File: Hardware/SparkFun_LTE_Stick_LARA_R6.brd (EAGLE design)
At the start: 25.4 x 82.5 mm, 133 parts, among them IC1 SN74AVC4T774PW, IC3 SN74AVC4T774PW, J1 NANO_SIM, U1 LARA-R6401, U2 AP7361C-33

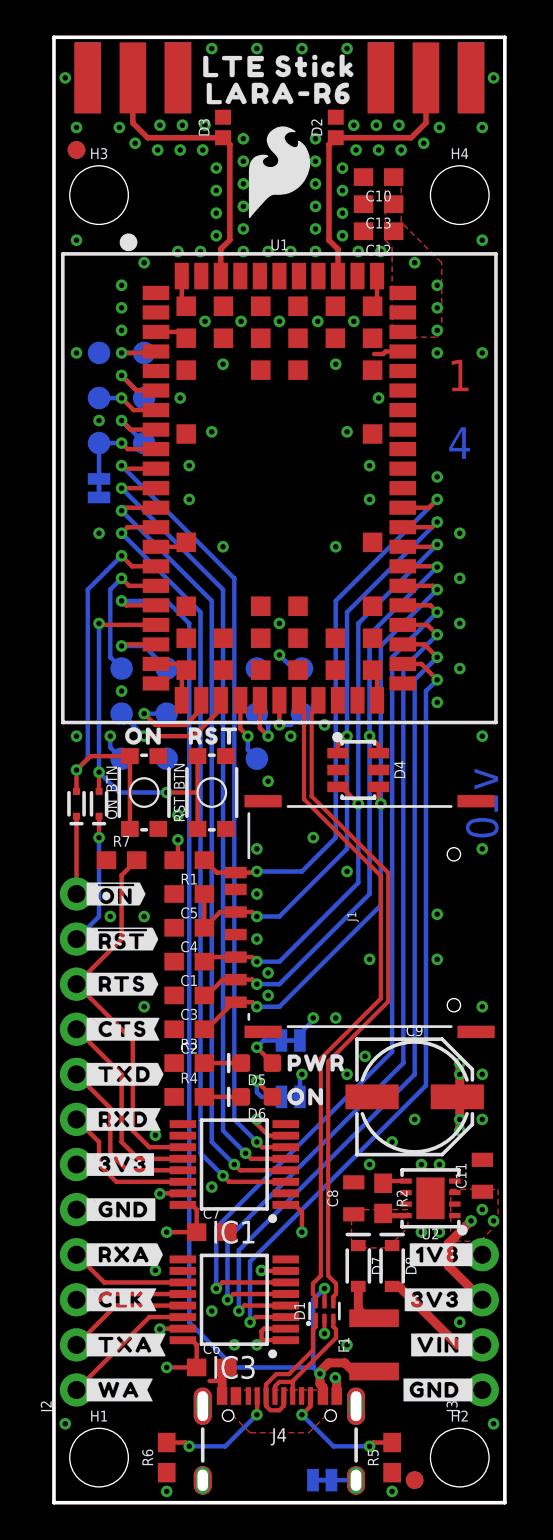
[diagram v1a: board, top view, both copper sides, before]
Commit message: v11 - Label SMA connectors in silkscreen
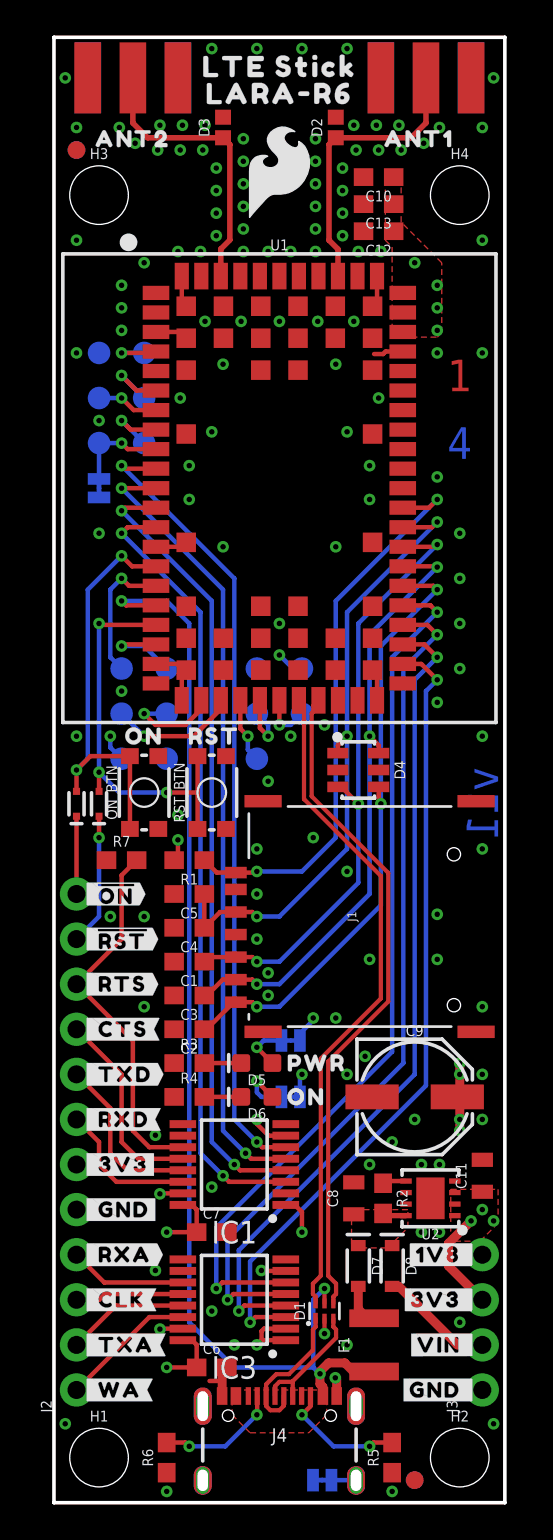
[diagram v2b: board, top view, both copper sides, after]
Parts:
- added U$29, U$36: (no value), output:ANT10
- added U$61, U$62: (no value), output:ANT20
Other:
- board text added: "v11"
- board text removed: "v10"
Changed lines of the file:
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@@
 <dimension x1="0" y1="0" x2="0" y2="73.66" x3="-8.89" y3="36.83" textsize="1.778" textratio="15" layer="47" unit="inch"/>
 <dimension x1="0" y1="0" x2="0" y2="82.55" x3="-12.7" y3="41.275" textsize="1.778" textratio="15" layer="47" unit="inch"/>
-<text x="24.13" y="39.37" size="1.778" layer="16" font="vector" ratio="15" rot="SMR270" align="center">v10</text>
+<text x="24.13" y="39.37" size="1.778" layer="16" font="vector" ratio="15" rot="SMR270" align="center">v11</text>
 <text x="22.86" y="63.5" size="1.778" layer="1" font="vector" ratio="15" rot="SR0" align="center">1</text>
 <text x="22.86" y="62.23" size="1.778" layer="2" font="vector" ratio="15" rot="SR0" align="center">2</text>
@@
 <element name="FRAME1" library="SparkFun-Aesthetics" package="CREATIVE_COMMONS" value="FRAME-LEDGER" x="-10.16" y="-25.4" smashed="yes">
 <attribute name="DESIGNER" value="Dryw Wade" x="-10.16" y="-25.4" size="1.778" layer="27" display="off"/>
-<attribute name="REV" value="v10" x="-10.16" y="-25.4" size="1.778" layer="27" display="off"/>
+<attribute name="REV" value="v11" x="-10.16" y="-25.4" size="1.778" layer="27" display="off"/>
 </element>
 <element name="U$56" library="output" package="UART20" value="" x="3.81" y="66.675" smashed="yes" rot="MR0"/>
@@
 <element name="U$53" library="output" package="#ON_LED#0" value="" x="14.224" y="22.86" smashed="yes" rot="MR0"/>
 <element name="U$60" library="output" package="#PWR_LED#0" value="" x="14.224" y="26.035" smashed="yes" rot="MR0"/>
+<element name="U$29" library="output" package="ANT10" value="" x="20.574" y="76.835" smashed="yes"/>
+<element name="U$36" library="output" package="ANT10" value="" x="21.082" y="76.835" smashed="yes" rot="MR0"/>
+<element name="U$61" library="output" package="ANT20" value="" x="4.699" y="76.835" smashed="yes" rot="MR0"/>
+<element name="U$62" library="output" package="ANT20" value="" x="4.445" y="76.835" smashed="yes"/>
 </elements>
 <signals>
